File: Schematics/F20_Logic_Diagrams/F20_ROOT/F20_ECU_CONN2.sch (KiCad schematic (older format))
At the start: 1 part, among them U5 ECU_Conn2

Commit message: 02/19/20 update
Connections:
- net FBPS: now reaches U5.12 (Analog17_In)
- net RBPS: now reaches U5.13 (Analog18_In)
- net BL_SW: now reaches U5.14 (Analog19_In)
- net ECU_+5V_Aux_Out1: now reaches U5.22 (+5V_Aux_Out)
- net ECU_AGND_1: now reaches U5.32 (AGround)
- net BL_SIG: now reaches U5.55 (HighsideSwitch_2)
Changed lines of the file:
@@
 Text Notes 7750 1350 0    100  ~ 20
 SHOULD ORGANIZE SENSORS, AUX\nPOWER +5V, CAN, ETC ON SECOND\nCONNECTOR TO DISTRIBUTE WIRING\nBETWEEN CONNECTORS
+Wire Wire Line
+	3000 4650 4500 4650
+Text GLabel 3000 4650 0    50   Output ~ 0
+ECU_+5V_Aux_Out1
+Text GLabel 7500 2250 2    50   Input ~ 0
+ECU_AGND_1
+Wire Wire Line
+	7500 2250 6000 2250
+Text GLabel 3000 3150 0    50   Input ~ 0
+FBPS
+Text GLabel 3000 3300 0    50   Input ~ 0
+RBPS
+Wire Wire Line
+	3000 3150 4500 3150
+Wire Wire Line
+	4500 3300 3000 3300
+Wire Wire Line
+	7550 5400 6000 5400
+Text GLabel 7550 5400 2    50   Output ~ 0
+BL_SIG
+Text GLabel 3000 3450 0    50   Input ~ 0
+BL_SW
+Wire Wire Line
+	3000 3450 4500 3450
 $EndSCHEMATC

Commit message: Added injectors drawing
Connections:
- no-connect marks 21 -> 17
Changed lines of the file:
@@
 $Descr A 11000 8500
 encoding utf-8
-Sheet 6 13
+Sheet 6 14
 Title "ECU Connector 2"
 Date "2020-02-18"
@@
 NoConn ~ 4500 2850
 NoConn ~ 4500 3000
-NoConn ~ 4500 5100
-NoConn ~ 4500 5250
-NoConn ~ 4500 5400
-NoConn ~ 4500 5550
 Text Notes 7750 1350 0    100  ~ 20
 SHOULD ORGANIZE SENSORS, AUX\nPOWER +5V, CAN, ETC ON SECOND\nCONNECTOR TO DISTRIBUTE WIRING\nBETWEEN CONNECTORS

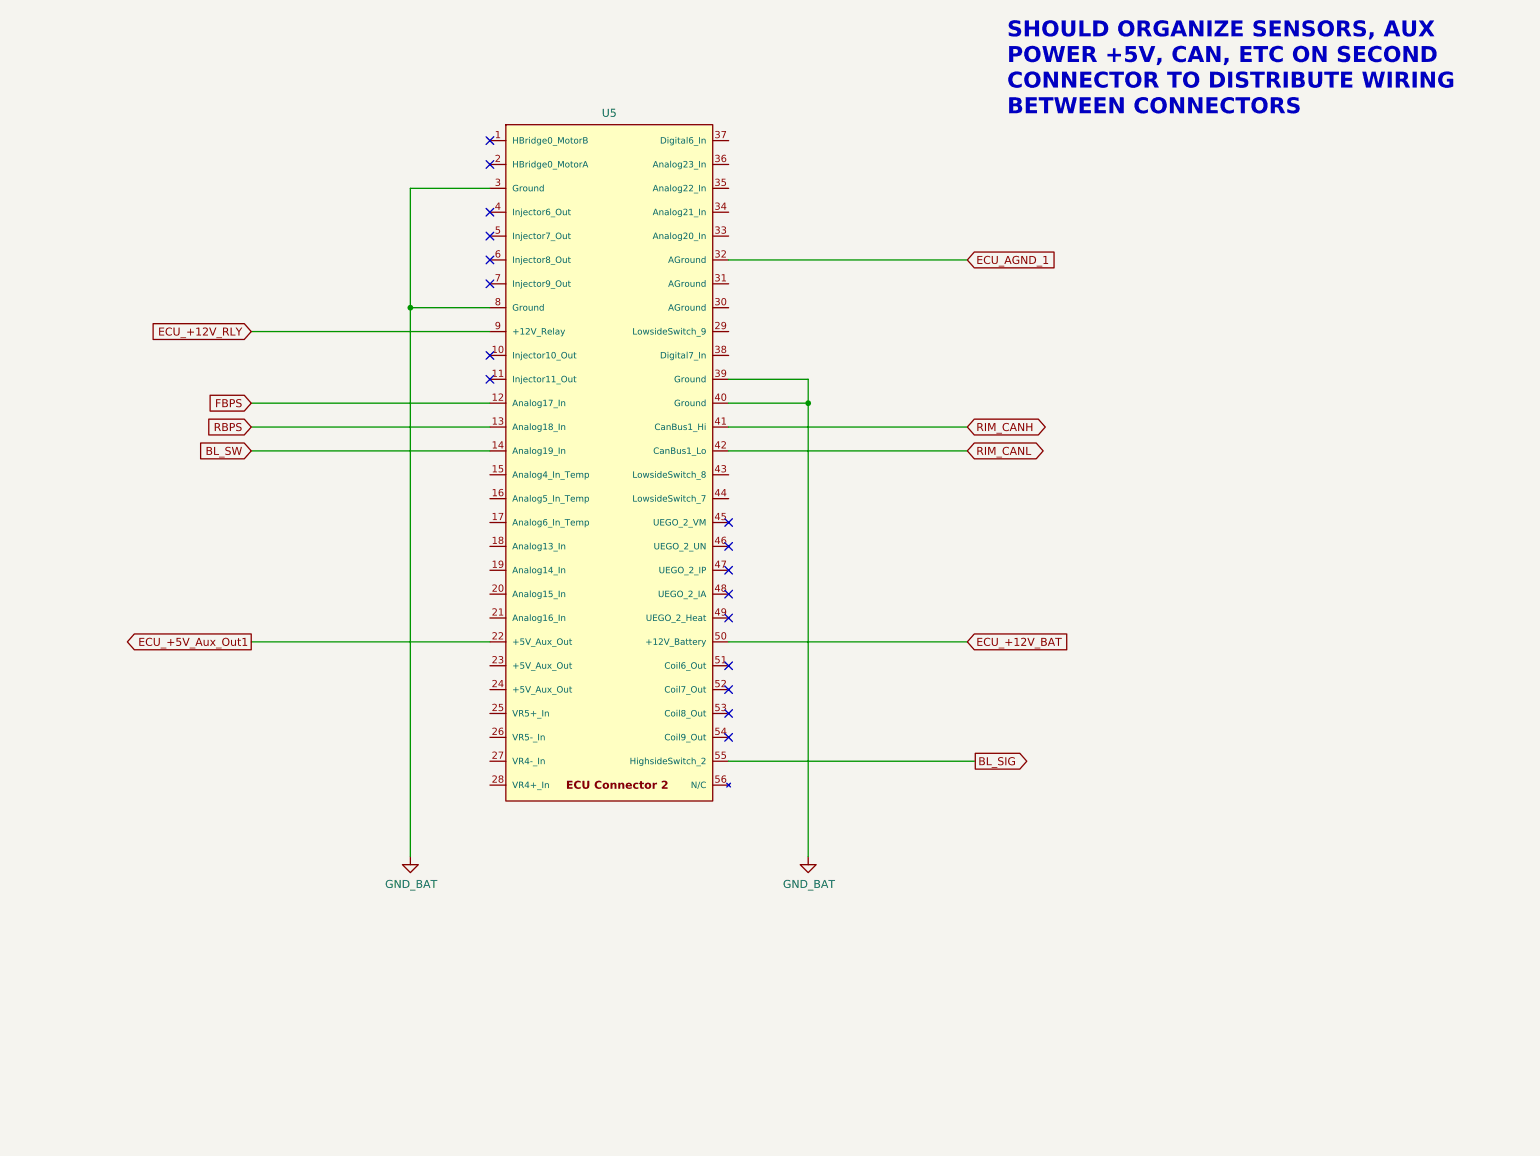
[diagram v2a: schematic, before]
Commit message: Major powertrain update, added shifting schematic
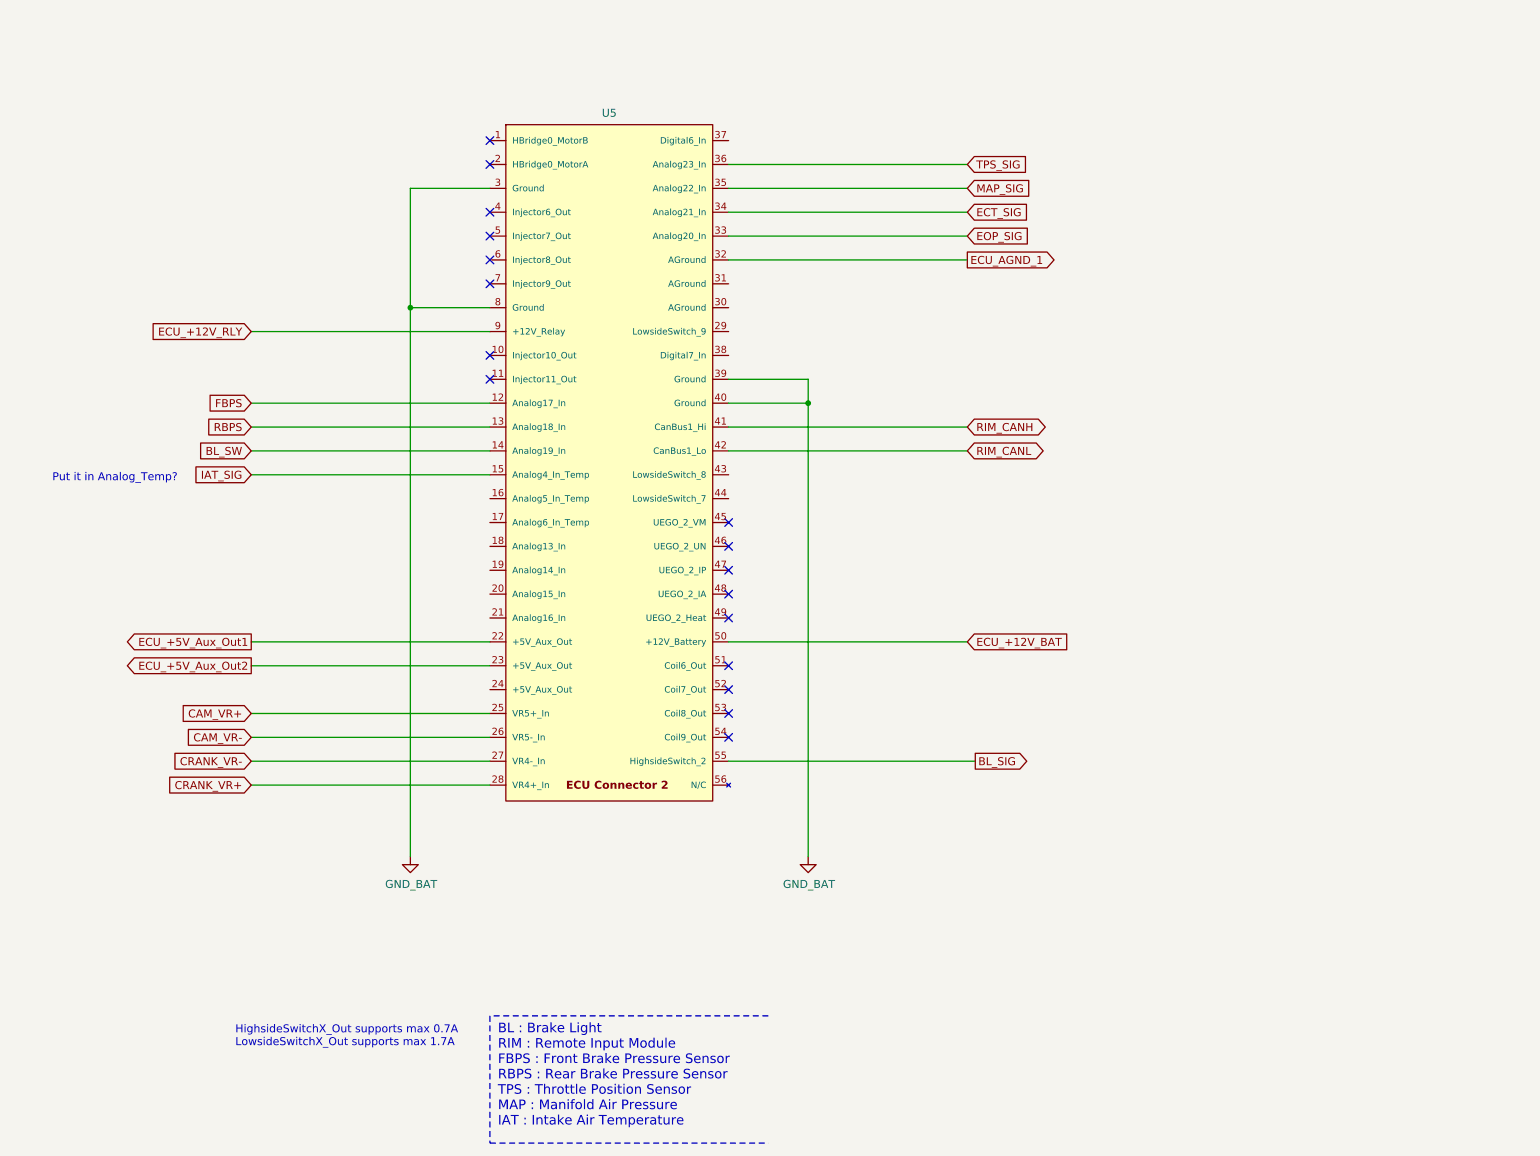
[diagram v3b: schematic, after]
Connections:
- net IAT_SIG: now reaches U5.15 (Analog4_In_Temp)
- net ECU_+5V_Aux_Out2: now reaches U5.23 (+5V_Aux_Out)
- net CAM_VR+: now reaches U5.25 (VR5+_In)
- net CAM_VR-: now reaches U5.26 (VR5-_In)
- net CRANK_VR-: now reaches U5.27 (VR4-_In)
- net CRANK_VR+: now reaches U5.28 (VR4+_In)
- net EOP_SIG: now reaches U5.33 (Analog20_In)
- net ECT_SIG: now reaches U5.34 (Analog21_In)
- net MAP_SIG: now reaches U5.35 (Analog22_In)
- net TPS_SIG: now reaches U5.36 (Analog23_In)
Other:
- note added: "BL : Brake Light\nRIM : Remote Input Module\nFBPS : Front Brake Pressure Sensor\nRBPS : Rear Brake Pressure Sensor\nTPS : Throttle Position Sensor\nMAP : Manifold Air Pressure\nIAT : Intake Air Temperature"
- note added: "HighsideSwitchX_Out supports max 0.7A\nLowsideSwitchX_Out supports max 1.7A"
- note added: "Put it in Analog_Temp?"
- note removed: "SHOULD ORGANIZE SENSORS, AUX\nPOWER +5V, CAN, ETC ON SECOND\nCONNECTOR TO DISTRIBUTE WIRING\nBETWEEN CONNECTORS"
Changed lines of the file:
@@
 $Descr A 11000 8500
 encoding utf-8
-Sheet 6 14
+Sheet 6 15
 Title "ECU Connector 2"
-Date "2020-02-18"
+Date "2020-03-03"
 Rev "A"
 Comp "F20"
@@
 NoConn ~ 4500 2850
 NoConn ~ 4500 3000
-Text Notes 7750 1350 0    100  ~ 20
-SHOULD ORGANIZE SENSORS, AUX\nPOWER +5V, CAN, ETC ON SECOND\nCONNECTOR TO DISTRIBUTE WIRING\nBETWEEN CONNECTORS
 Wire Wire Line
 	3000 4650 4500 4650
 Text GLabel 3000 4650 0    50   Output ~ 0
 ECU_+5V_Aux_Out1
-Text GLabel 7500 2250 2    50   Input ~ 0
-ECU_AGND_1
 Wire Wire Line
 	7500 2250 6000 2250
@@
 Wire Wire Line
 	3000 3450 4500 3450
+Text GLabel 3000 4800 0    50   Output ~ 0
+ECU_+5V_Aux_Out2
+Wire Wire Line
+	3000 4800 4500 4800
+Text GLabel 7500 2250 2    50   Output ~ 0
+ECU_AGND_1
+Text Notes 4550 7700 0    60   ~ 0
+BL : Brake Light\nRIM : Remote Input Module\nFBPS : Front Brake Pressure Sensor\nRBPS : Rear Brake Pressure Sensor\nTPS : Throttle Position Sensor\nMAP : Manifold Air Pressure\nIAT : Intake Air Temperature
+Wire Notes Line
+	6250 7000 4500 7000
+Wire Notes Line
+	4500 7000 4500 7800
+Text GLabel 3000 5100 0    50   Input ~ 0
+CAM_VR+
+Wire Wire Line
+	3000 5100 4500 5100
+Text GLabel 3000 5250 0    50   Input ~ 0
+CAM_VR-
+Wire Wire Line
+	3000 5250 4500 5250
+Text GLabel 3000 5400 0    50   Input ~ 0
+CRANK_VR-
+Wire Wire Line
+	3000 5400 4500 5400
+Text GLabel 3000 5550 0    50   Input ~ 0
+CRANK_VR+
+Wire Wire Line
+	3000 5550 4500 5550
+Text GLabel 3000 3600 0    50   Input ~ 0
+IAT_SIG
+Wire Wire Line
+	3000 3600 4500 3600
+Text Notes 1750 3650 0    50   ~ 0
+Put it in Analog_Temp?
+Text GLabel 7500 1650 2    50   Input ~ 0
+TPS_SIG
+Wire Wire Line
+	7500 1650 6000 1650
+Text GLabel 7500 1800 2    50   Input ~ 0
+MAP_SIG
+Wire Wire Line
+	7500 1800 6000 1800
+Wire Notes Line
+	4500 7800 6250 7800
+Text GLabel 7500 1950 2    50   Input ~ 0
+ECT_SIG
+Wire Wire Line
+	7500 1950 6000 1950
+Text GLabel 7500 2100 2    50   Input ~ 0
+EOP_SIG
+Wire Wire Line
+	7500 2100 6000 2100
+Text Notes 2900 7200 0    50   ~ 0
+HighsideSwitchX_Out supports max 0.7A\nLowsideSwitchX_Out supports max 1.7A
 $EndSCHEMATC

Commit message: Update
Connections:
- net UP_SHIFT_CTRL: now reaches U5.29 (LowsideSwitch_9)
- net DOWN_SHIFT_CTRL: now reaches U5.43 (LowsideSwitch_8)
- net CLUTCH_CTRL: now reaches U5.44 (LowsideSwitch_7)
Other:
- note added: "4A max (0.416A used)"
- note added: "4A max (0.542*3=1.625A used)"
- note added: "LowsideSwitch7/8/9_Out supports max 4A\nand have flyback diodes"
- note removed: "HighsideSwitchX_Out supports max 0.7A\nLowsideSwitchX_Out supports max 1.7A"
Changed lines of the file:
@@
 EESchema Schematic File Version 4
-LIBS:F20_ROOT-cache
 EELAYER 30 0
 EELAYER END
@@
 Wire Wire Line
 	7500 2100 6000 2100
-Text Notes 2900 7200 0    50   ~ 0
-HighsideSwitchX_Out supports max 0.7A\nLowsideSwitchX_Out supports max 1.7A
+Text Notes 2800 7200 0    50   ~ 0
+LowsideSwitch7/8/9_Out supports max 4A\nand have flyback diodes
+Text GLabel 7500 2700 2    50   Output ~ 0
+UP_SHIFT_CTRL
+Wire Wire Line
+	7500 2700 6000 2700
+Text Notes 8150 2750 0    50   ~ 0
+4A max (0.416A used)
+Text Notes 8250 3650 0    50   ~ 0
+4A max (0.416A used)
+Text GLabel 7500 3600 2    50   Output ~ 0
+DOWN_SHIFT_CTRL
+Wire Wire Line
+	7500 3600 6000 3600
+Text GLabel 7500 3750 2    50   Output ~ 0
+CLUTCH_CTRL
+Wire Wire Line
+	7500 3750 6000 3750
+Text Notes 8100 3800 0    50   ~ 0
+4A max (0.542*3=1.625A used)
 $EndSCHEMATC

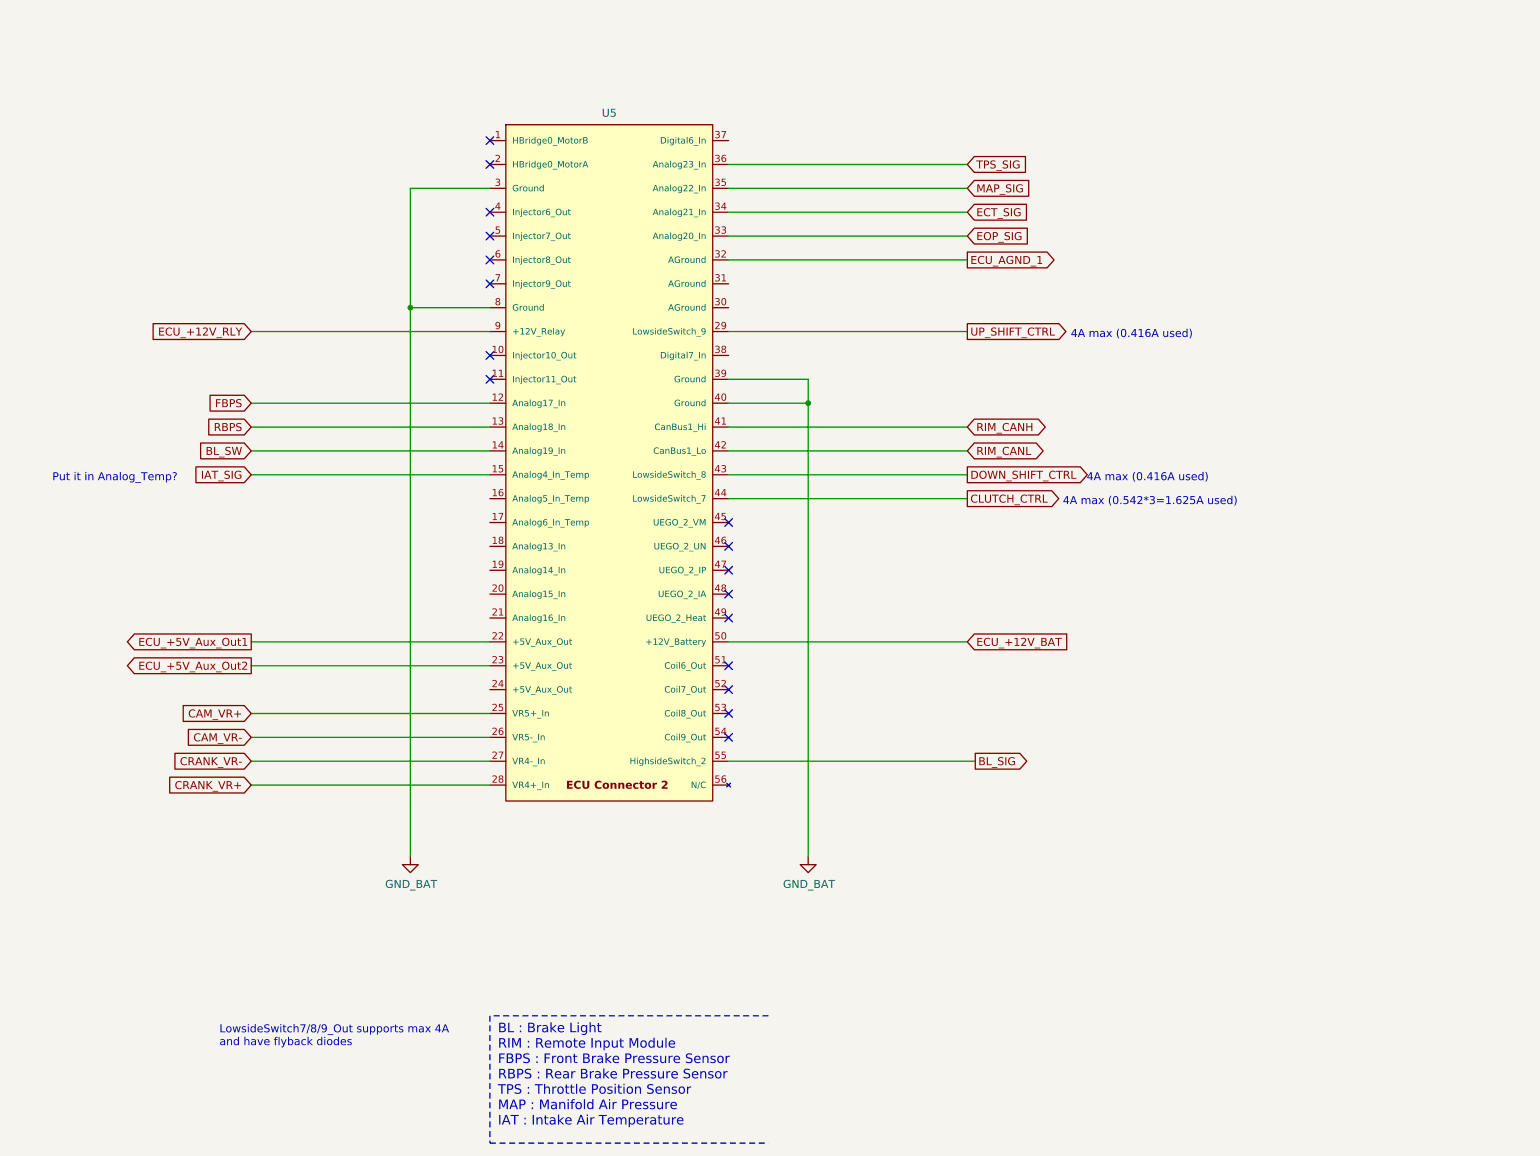
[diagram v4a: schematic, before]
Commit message: Added steering wheel drawing, udpated some ECU pinout to match previous tune, added accel/XBEE drawing
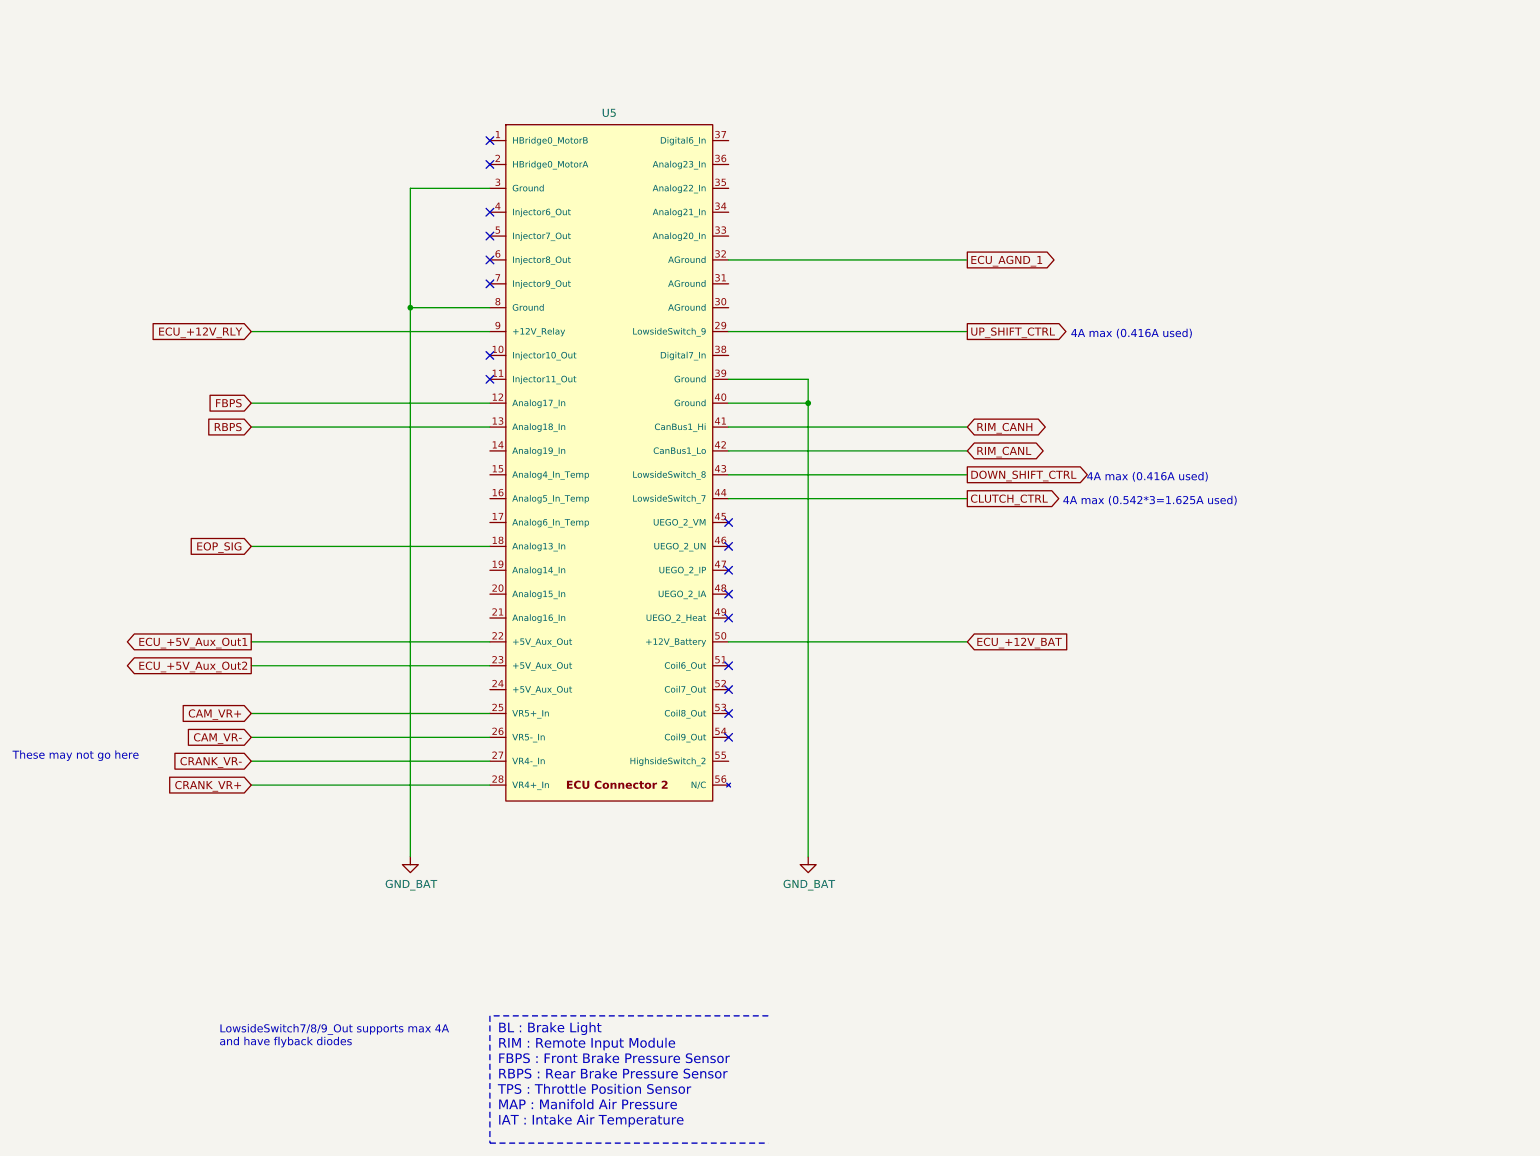
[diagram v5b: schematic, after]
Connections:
- net EOP_SIG: now also U5.18 (Analog13_In); no longer U5.33 (Analog20_In)
- net BL_SIG: no longer names the net of U5.55 (HighsideSwitch_2)
- net BL_SW: no longer names the net of U5.14 (Analog19_In)
- net ECT_SIG: no longer names the net of U5.34 (Analog21_In)
- net IAT_SIG: no longer names the net of U5.15 (Analog4_In_Temp)
- net MAP_SIG: no longer names the net of U5.35 (Analog22_In)
- net TPS_SIG: no longer names the net of U5.36 (Analog23_In)
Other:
- note added: "These may not go here"
- note removed: "Put it in Analog_Temp?"
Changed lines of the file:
@@
 EESchema Schematic File Version 4
+LIBS:F20_ROOT-cache
 EELAYER 30 0
 EELAYER END
 $Descr A 11000 8500
 encoding utf-8
-Sheet 6 15
+Sheet 6 18
 Title "ECU Connector 2"
 Date "2020-03-03"
@@
 Wire Wire Line
 	4500 3300 3000 3300
-Wire Wire Line
-	7550 5400 6000 5400
-Text GLabel 7550 5400 2    50   Output ~ 0
-BL_SIG
-Text GLabel 3000 3450 0    50   Input ~ 0
-BL_SW
-Wire Wire Line
-	3000 3450 4500 3450
 Text GLabel 3000 4800 0    50   Output ~ 0
 ECU_+5V_Aux_Out2
@@
 Wire Wire Line
 	3000 5550 4500 5550
-Text GLabel 3000 3600 0    50   Input ~ 0
-IAT_SIG
-Wire Wire Line
-	3000 3600 4500 3600
-Text Notes 1750 3650 0    50   ~ 0
-Put it in Analog_Temp?
-Text GLabel 7500 1650 2    50   Input ~ 0
-TPS_SIG
-Wire Wire Line
-	7500 1650 6000 1650
-Text GLabel 7500 1800 2    50   Input ~ 0
-MAP_SIG
-Wire Wire Line
-	7500 1800 6000 1800
 Wire Notes Line
 	4500 7800 6250 7800
-Text GLabel 7500 1950 2    50   Input ~ 0
-ECT_SIG
-Wire Wire Line
-	7500 1950 6000 1950
-Text GLabel 7500 2100 2    50   Input ~ 0
+Text GLabel 3000 4050 0    50   Input ~ 0
 EOP_SIG
-Wire Wire Line
-	7500 2100 6000 2100
 Text Notes 2800 7200 0    50   ~ 0
 LowsideSwitch7/8/9_Out supports max 4A\nand have flyback diodes
@@
 Text Notes 8100 3800 0    50   ~ 0
 4A max (0.542*3=1.625A used)
+Text Notes 1500 5400 0    50   ~ 0
+These may not go here
+Wire Wire Line
+	3000 4050 4500 4050
 $EndSCHEMATC
